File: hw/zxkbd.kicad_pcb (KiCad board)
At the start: 2 copper layers, 148 x 48 mm, 55 parts, among them J1 TAPE, J3 AY_IN, J4 SCART, J5 SERIAL, J6 ISP, Q1 BC846, SW1 RESET, SW2 MAGIC, SW3 AVR_RST, U1 74HC373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

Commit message: PCB first pass
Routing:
- net /D4: track 0.00 -> 183.7 mm, vias 0 -> 17
- net /KDA4: track 8.83 -> 128.7 mm, vias 0 -> 2
- net /KDB4: track 7.84 -> 112.5 mm, vias 0 -> 4
- net /KDB2: track 7.78 -> 103.0 mm, vias 0 -> 4
- net /KDA2: track 8.89 -> 100.4 mm, vias 0 -> 2
- net /KDD3: track 7.77 -> 99.1 mm, vias 0 -> 2
- net /KA0: track 3.39 -> 93.5 mm, vias 0 -> 2
- net /KA1: track 2.88 -> 89.2 mm, vias 0 -> 2
- net /KDA1: track 9.02 -> 92.0 mm, vias 0 -> 2
- net /PCLK: track 0.00 -> 75.1 mm, vias 0 -> 3
- net /KA3: track 3.38 -> 77.1 mm, vias 0 -> 2
- net /KDB1: track 7.90 -> 77.3 mm, vias 0 -> 2
- net /KDD2: track 7.64 -> 75.6 mm, vias 0 -> 4
- net /PDATA: track 0.00 -> 63.1 mm, vias 0 -> 1
- net /KDA0: track 8.98 -> 70.6 mm, vias 0 -> 2
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
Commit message: via stitching
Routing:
- net GND: track 3.99 -> 24.3 mm, vias 2 -> 65
- net /KDD3: track 99.1 -> 102.0 mm
- net /KA6: track 56.8 -> 59.4 mm
- net /D2: track 165.2 -> 167.1 mm
- net /KDE3: track 85.5 -> 87.4 mm
- net /KA2: track 49.5 -> 51.1 mm
- net /KDG3: track 51.4 -> 52.9 mm
- net /KDH3: track 41.4 -> 42.8 mm
- net /KDF3: track 74.0 -> 75.4 mm
- net /D1: track 172.3 -> 173.7 mm
- net /KDC0: track 45.0 -> 45.8 mm
- net /KA1: track 89.2 -> 90.1 mm
- net /KDB2: track 103.0 -> 103.8 mm
- net /KDH2: track 52.7 -> 53.5 mm
- net /KA3: track 77.1 -> 77.8 mm
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- added copper zone on B.Cu, net GND
- added copper zone on F.Cu, net GND

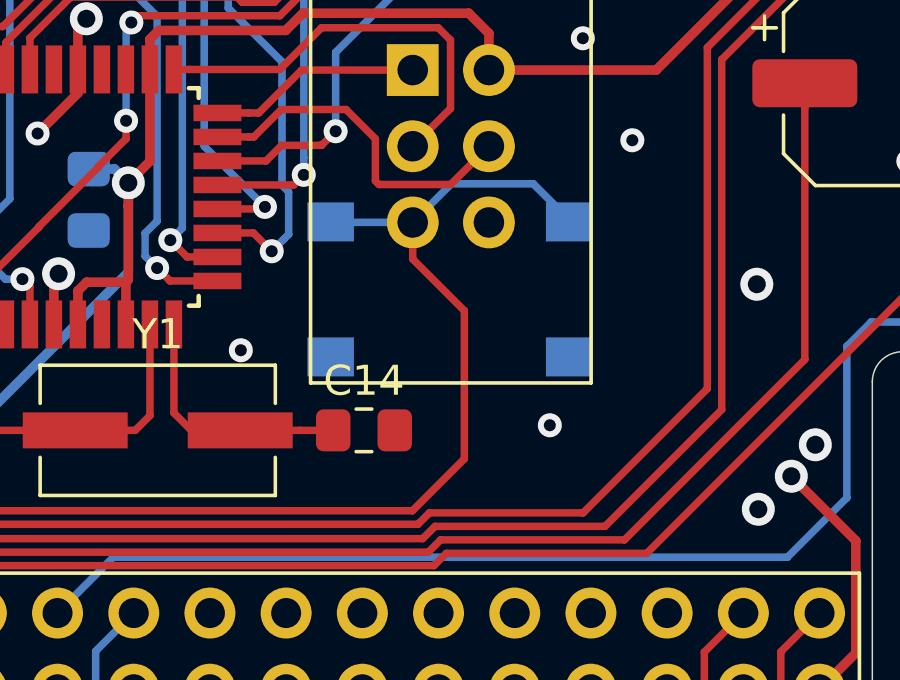
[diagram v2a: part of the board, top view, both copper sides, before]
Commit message: fixed PCB mistake, AVR reset switch overlapped with ISP header pins on the back side of the board.
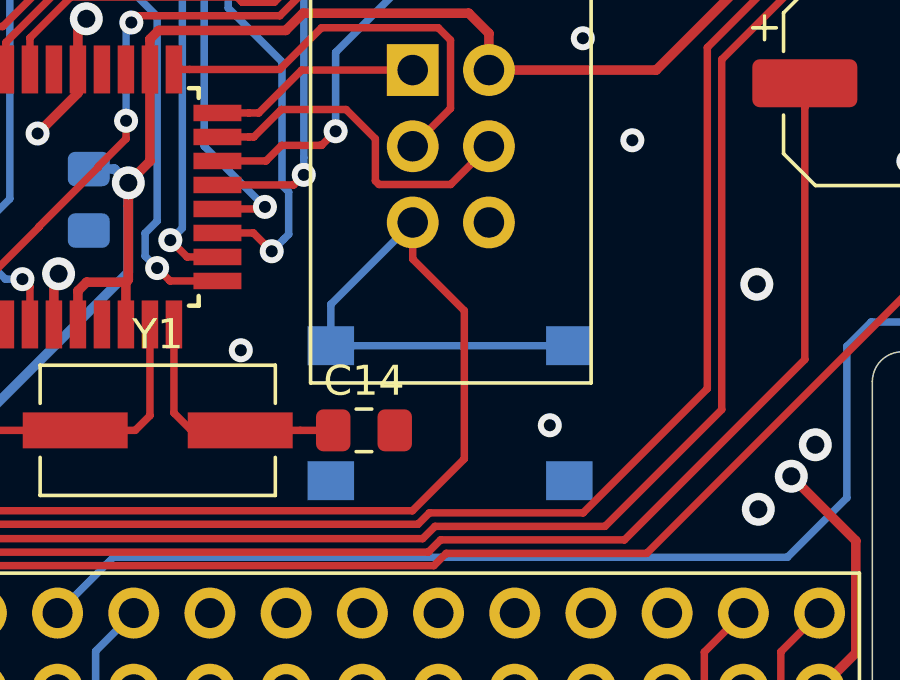
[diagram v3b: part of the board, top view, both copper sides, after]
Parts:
- moved SW3 4.13 mm to (174.4, 139.1)
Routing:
- net /~RESET: track 57.1 -> 61.3 mm
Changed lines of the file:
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@@
     (thickness 1.6)
     (drawings 13)
-    (tracks 2804)
+    (tracks 2801)
     (zones 0)
     (modules 55)
@@
   )
   (module Button_Switch_SMD:SW_Push_1P1T_NO_6x6mm_H9.5mm (layer B.Cu)
-    (at 174.42 134.92)
+    (at 174.425 139.05)
     (descr "tactile push button, 6x6mm e.g. PTS645xx series, height=9.5mm")
     (tags "tact sw push 6mm smd")
@@
   (segment (start 171.935002 131.305) (end 171.935002 129.901998) (width 0.25) (layer F.Cu) (net 23))
   (segment (start 174.445 131.425) (end 172.055002 131.425) (width 0.25) (layer F.Cu) (net 23))
-  (segment (start 170.465 132.69) (end 170.445 132.67) (width 0.25) (layer B.Cu) (net 24))
-  (segment (start 173.18 132.69) (end 170.465 132.69) (width 0.25) (layer B.Cu) (net 24))
   (segment (start 173.18 133.911314) (end 174.9 135.631314) (width 0.25) (layer F.Cu) (net 24))
   (segment (start 173.18 132.69) (end 173.18 133.911314) (width 0.25) (layer F.Cu) (net 24))
@@
   (segment (start 152.84 132.24) (end 158.17 132.24) (width 0.25) (layer F.Cu) (net 24))
   (segment (start 151.51 133.57) (end 152.84 132.24) (width 0.25) (layer F.Cu) (net 24))
-  (segment (start 178.41 132.61) (end 178.44 132.61) (width 0.25) (layer B.Cu) (net 24))
-  (segment (start 177.2 131.4) (end 178.41 132.61) (width 0.25) (layer B.Cu) (net 24))
-  (segment (start 173.18 132.69) (end 174.47 131.4) (width 0.25) (layer B.Cu) (net 24))
-  (segment (start 174.47 131.4) (end 177.2 131.4) (width 0.25) (layer B.Cu) (net 24))
+  (segment (start 170.45 135.42) (end 170.45 136.8) (width 0.25) (layer B.Cu) (net 24))
+  (segment (start 173.18 132.69) (end 170.45 135.42) (width 0.25) (layer B.Cu) (net 24))
+  (segment (start 170.45 136.8) (end 178.4 136.8) (width 0.25) (layer B.Cu) (net 24))
   (segment (start 202 117.4) (end 202 119.3) (width 0.25) (layer F.Cu) (net 25) (status 30))
   (segment (start 202 123.55) (end 202 121.2) (width 0.25) (layer F.Cu) (net 26) (status 30))

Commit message: finishing the pcb
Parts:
- added C15: 0.1uF, Capacitor_SMD:C_0805_2012Metric_Pad1.15x1.40mm_HandSolder, B.Cu at (86.6, 130.4)
- added C16: 0.1uF, Capacitor_SMD:C_0805_2012Metric_Pad1.15x1.40mm_HandSolder, B.Cu at (111.9, 132.6)
- added C17: 0.1uF, Capacitor_SMD:C_0805_2012Metric_Pad1.15x1.40mm_HandSolder, B.Cu at (133.6, 133.4)
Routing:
- net GND: track 24.3 -> 41.9 mm, vias 65 -> 73
- net VCC: track 505.1 -> 522.5 mm, vias 9 -> 12
- net /KDE0: track 38.3 -> 41.7 mm
- net /KDF0: track 29.7 -> 32.8 mm
- net /KDG0: track 68.6 -> 71.7 mm
- net /KDH0: track 80.9 -> 83.9 mm
- net /KDB4: track 112.5 -> 113.6 mm
- net /D0: track 183.8 -> 184.9 mm
- net /KA1: track 90.1 -> 89.0 mm
- net /SEL2: track 58.0 -> 58.7 mm
- net Net-(SW1-Pad2): track 140.2 -> 139.6 mm
- net /KDG3: track 52.9 -> 52.4 mm
- net /KDB3: track 111.7 -> 111.2 mm
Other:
- board text added: "AVR ISP"
- board text added: "GND"
- board text added: "RXD"
- board text added: "TXD"
- board text added: "VCC"
- board text added: "zxkbd rev 1"
- board text added: "zxkbd rev 1 Copyright © 2020 John Tsiombikas <nuclear@member.fsf.org> Creative Commons Attribution Share-Alike (CC BY-SA) https://github.com/jtsiomb/zxkbd"

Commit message: labels on the pcb
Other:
- board text added: "BLUE"
- board text added: "GREEN"
- board text added: "H+V SYNC"
- board text added: "KA3"
- board text added: "KA3-KA0"
- board text added: "KA4"
- board text added: "KA5"
- board text added: "KA6"
- board text added: "KA7"
- board text added: "KD0"
- board text added: "KD1"
- board text added: "KD2"
- board text added: "KD3"
- board text added: "KD4"
- board text added: "RED"
- board text added: "SOUND"
- board text added: "TAP IN"
- board text added: "TAP OUT"
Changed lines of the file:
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@@
   (general
     (thickness 1.6)
-    (drawings 20)
+    (drawings 43)
     (tracks 2889)
     (zones 0)
@@
     (tags "resistor array")
     (attr smd)
-    (fp_text reference RN6 (at 0 4.2 270) (layer B.SilkS)
+    (fp_text reference RN6 (at 0.8 -4.14 90) (layer B.SilkS)
       (effects (font (size 1 1) (thickness 0.15)) (justify mirror))
     )
-    (fp_text value 4k7 (at 0 -4.2 270) (layer B.Fab)
+    (fp_text value 4k7 (at 0 -0.04) (layer B.SilkS)
       (effects (font (size 1 1) (thickness 0.15)) (justify mirror))
     )
+    (fp_line (start 2.2 -3.45) (end -2.21 -3.45) (layer B.CrtYd) (width 0.05))
+    (fp_line (start 2.2 -3.45) (end 2.2 3.45) (layer B.CrtYd) (width 0.05))
+    (fp_line (start -2.21 3.45) (end -2.21 -3.45) (layer B.CrtYd) (width 0.05))
+    (fp_line (start -2.21 3.45) (end 2.2 3.45) (layer B.CrtYd) (width 0.05))
+    (fp_line (start 1.05 3.27) (end -1.05 3.27) (layer B.SilkS) (width 0.12))
+    (fp_line (start 1.05 -3.27) (end -1.05 -3.27) (layer B.SilkS) (width 0.12))
+    (fp_line (start -1.6 -3.2) (end -1.6 3.2) (layer B.Fab) (width 0.1))
+    (fp_line (start 1.6 -3.2) (end -1.6 -3.2) (layer B.Fab) (width 0.1))
+    (fp_line (start 1.6 3.2) (end 1.6 -3.2) (layer B.Fab) (width 0.1))
+    (fp_line (start -1.6 3.2) (end 1.6 3.2) (layer B.Fab) (width 0.1))
     (fp_text user %R (at 0 0) (layer B.Fab)
       (effects (font (size 1 1) (thickness 0.15)) (justify mirror))
     )
-    (fp_line (start -1.6 3.2) (end 1.6 3.2) (layer B.Fab) (width 0.1))
-    (fp_line (start 1.6 3.2) (end 1.6 -3.2) (layer B.Fab) (width 0.1))
-    (fp_line (start 1.6 -3.2) (end -1.6 -3.2) (layer B.Fab) (width 0.1))
-    (fp_line (start -1.6 -3.2) (end -1.6 3.2) (layer B.Fab) (width 0.1))
-    (fp_line (start 1.05 -3.27) (end -1.05 -3.27) (layer B.SilkS) (width 0.12))
-    (fp_line (start 1.05 3.27) (end -1.05 3.27) (layer B.SilkS) (width 0.12))
-    (fp_line (start -2.21 3.45) (end 2.2 3.45) (layer B.CrtYd) (width 0.05))
-    (fp_line (start -2.21 3.45) (end -2.21 -3.45) (layer B.CrtYd) (width 0.05))
-    (fp_line (start 2.2 -3.45) (end 2.2 3.45) (layer B.CrtYd) (width 0.05))
-    (fp_line (start 2.2 -3.45) (end -2.21 -3.45) (layer B.CrtYd) (width 0.05))
-    (pad 1 smd rect (at -1.5 2.6 90) (size 0.9 0.9) (layers B.Cu B.Paste B.Mask)
-      (net 69 /KA0))
-    (pad 5 smd rect (at -1.5 -2.6 90) (size 0.9 0.9) (layers B.Cu B.Paste B.Mask)
-      (net 2 VCC))
-    (pad 2 smd rect (at -1.5 1.28 90) (size 0.9 0.9) (layers B.Cu B.Paste B.Mask)
-      (net 70 /KA1))
-    (pad 4 smd rect (at -1.5 -1.28 90) (size 0.9 0.9) (layers B.Cu B.Paste B.Mask)
-      (net 71 /KA3))
-    (pad 3 smd rect (at -1.5 0 90) (size 0.9 0.9) (layers B.Cu B.Paste B.Mask)
-      (net 72 /KA2))
-    (pad 7 smd rect (at 1.5 -1.28 90) (size 0.9 0.9) (layers B.Cu B.Paste B.Mask)
-      (net 73 /KA5))
-    (pad 10 smd rect (at 1.5 2.6 90) (size 0.9 0.9) (layers B.Cu B.Paste B.Mask))
-    (pad 6 smd rect (at 1.5 -2.6 90) (size 0.9 0.9) (layers B.Cu B.Paste B.Mask)
-      (net 74 /KA4))
-    (pad 9 smd rect (at 1.5 1.28 90) (size 0.9 0.9) (layers B.Cu B.Paste B.Mask)
-      (net 75 /KA7))
     (pad 8 smd rect (at 1.5 0 90) (size 0.9 0.9) (layers B.Cu B.Paste B.Mask)
       (net 76 /KA6))
+    (pad 9 smd rect (at 1.5 1.28 90) (size 0.9 0.9) (layers B.Cu B.Paste B.Mask)
+      (net 75 /KA7))
+    (pad 6 smd rect (at 1.5 -2.6 90) (size 0.9 0.9) (layers B.Cu B.Paste B.Mask)
+      (net 74 /KA4))
+    (pad 10 smd rect (at 1.5 2.6 90) (size 0.9 0.9) (layers B.Cu B.Paste B.Mask))
+    (pad 7 smd rect (at 1.5 -1.28 90) (size 0.9 0.9) (layers B.Cu B.Paste B.Mask)
+      (net 73 /KA5))
+    (pad 3 smd rect (at -1.5 0 90) (size 0.9 0.9) (layers B.Cu B.Paste B.Mask)
+      (net 72 /KA2))
+    (pad 4 smd rect (at -1.5 -1.28 90) (size 0.9 0.9) (layers B.Cu B.Paste B.Mask)
+      (net 71 /KA3))
+    (pad 2 smd rect (at -1.5 1.28 90) (size 0.9 0.9) (layers B.Cu B.Paste B.Mask)
+      (net 70 /KA1))
+    (pad 5 smd rect (at -1.5 -2.6 90) (size 0.9 0.9) (layers B.Cu B.Paste B.Mask)
+      (net 2 VCC))
+    (pad 1 smd rect (at -1.5 2.6 90) (size 0.9 0.9) (layers B.Cu B.Paste B.Mask)
+      (net 69 /KA0))
     (model ${KISYS3DMOD}/Resistor_SMD.3dshapes/R_Array_Convex_5x1206.wrl
       (at (xyz 0 0 0))
@@
     )
   )
+  (gr_text "TAP OUT" (at 187.3 141.2 270) (layer B.SilkS)
+    (effects (font (size 1 1) (thickness 0.15)) (justify mirror))
+  )
+  (gr_text "TAP IN" (at 183.5 141.9 270) (layer B.SilkS)
+    (effects (font (size 1 1) (thickness 0.15)) (justify mirror))
+  )
+  (gr_text SOUND (at 161.3 141.8 270) (layer B.SilkS)
+    (effects (font (size 1 1) (thickness 0.15)) (justify mirror))
+  )
+  (gr_text GREEN (at 153.7 142 270) (layer B.SilkS)
+    (effects (font (size 1 1) (thickness 0.15)) (justify mirror))
+  )
+  (gr_text BLUE (at 151.1 142.6 270) (layer B.SilkS)
+    (effects (font (size 1 1) (thickness 0.15)) (justify mirror))
+  )
+  (gr_text RED (at 148.6 143 270) (layer B.SilkS)
+    (effects (font (size 1 1) (thickness 0.15)) (justify mirror))
+  )
+  (gr_text "H+V SYNC" (at 146.1 140.6 270) (layer B.SilkS)
+    (effects (font (size 1 1) (thickness 0.15)) (justify mirror))
+  )
+  (gr_text KD0 (at 138.5 143 270) (layer B.SilkS)
+    (effects (font (size 1 1) (thickness 0.15)) (justify mirror))
+  )
+  (gr_text KD1 (at 135.9 143 270) (layer B.SilkS)
+    (effects (font (size 1 1) (thickness 0.15)) (justify mirror))
+  )
+  (gr_text KD2 (at 133.3 143 270) (layer B.SilkS)
+    (effects (font (size 1 1) (thickness 0.15)) (justify mirror))
+  )
+  (gr_text KD4 (at 130.9 143 270) (layer B.SilkS)
+    (effects (font (size 1 1) (thickness 0.15)) (justify mirror))
+  )
+  (gr_text KD3 (at 128.3 143 270) (layer B.SilkS)
+    (effects (font (size 1 1) (thickness 0.15)) (justify mirror))
+  )
+  (gr_text KA7 (at 125.8 143.1 270) (layer B.SilkS)
+    (effects (font (size 1 1) (thickness 0.15)) (justify mirror))
+  )
+  (gr_text KA3 (at 105.8 145.6 270) (layer B.SilkS)
+    (effects (font (size 1 1) (thickness 0.15)) (justify mirror))
+  )
+  (gr_text KA6 (at 123.3 143.1 270) (layer B.SilkS)
+    (effects (font (size 1 1) (thickness 0.15)) (justify mirror))
+  )
+  (gr_text KA5 (at 120.7 143.1 270) (layer B.SilkS)
+    (effects (font (size 1 1) (thickness 0.15)) (justify mirror))
+  )
+  (gr_text KA4 (at 118.2 143.1 270) (layer B.SilkS)
+    (effects (font (size 1 1) (thickness 0.15)) (justify mirror))
+  )
+  (gr_line (start 107.3 144.4) (end 107 144.7) (layer B.SilkS) (width 0.12))
+  (gr_line (start 116.3 144.4) (end 116.6 144.8) (layer B.SilkS) (width 0.12))
+  (gr_line (start 107.3 144.3) (end 116.3 144.4) (layer B.SilkS) (width 0.12))
+  (gr_line (start 107 143.8) (end 107.3 144.3) (layer B.SilkS) (width 0.12))
+  (gr_line (start 100.4 143.8) (end 107 143.8) (layer B.SilkS) (width 0.12))
+  (gr_text KA3-KA0 (at 103.6 143.1) (layer B.SilkS)
+    (effects (font (size 1 1) (thickness 0.15)) (justify mirror))
+  )
   (gr_text GND (at 150.9 138.6) (layer F.SilkS)

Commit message: PCB completed
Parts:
- added J2: LINEOUT, zxkbd:cui_sj1-3525ng, F.Cu at (222.3, 129.6)
- added REF**: OSHW-Logo2_9.8x8mm_SilkScreen, Symbol:OSHW-Logo2_9.8x8mm_SilkScreen, B.Cu at (166.1, 120.5)
- added REF**: OSHW-Logo2_9.8x8mm_SilkScreen, Symbol:OSHW-Logo2_9.8x8mm_SilkScreen, F.Cu at (143.8, 130.5)
- moved J3 39.7 mm to (183.5, 132.4), turned to 0 degrees
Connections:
- U8 pad A2: (no net) -> VCC
- U8 pad A27: (no net) -> GND
- U8 pad A28: (no net) -> GND
- U8 pad A29: (no net) -> GND
- U8 pad A30: (no net) -> GND
- U8 pad A31: (no net) -> GND
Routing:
- net /A_R: track 9.69 -> 22.9 mm
- net /GREEN: track 45.1 -> 53.3 mm
- net /A_L: track 9.84 -> 16.5 mm
- net Net-(J3-Pad1): track 28.2 -> 22.8 mm
- net Net-(J3-Pad3): track 18.9 -> 22.9 mm
- net VCC: track 522.5 -> 525.1 mm
- net /RED: track 61.0 -> 59.5 mm
- net /HVSYNC: track 72.6 -> 71.4 mm
- net /SOUND: track 56.4 -> 57.3 mm
- net GND: vias 73 -> 75
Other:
- board size 148 x 48 mm -> 148.3 x 48 mm
- board text added: "AU_IN"
- board text added: "AU_L"
- board text added: "AU_R"
- board text added: "AVR RESET"
- board text added: "CLK"
- board text added: "DATA"
- board text added: "L"
- board text added: "MAGIC"
- board text added: "PS/2 keyb"
- board text added: "Pentagon128k connector"
- board text added: "R"
- board text added: "RESET"
- board text added: "SCART"
- board text added: "SERIAL"
- board text added: "SYNC"
- board text added: "VCC AU_L AU_R GND GND"
- board text added: "VCC SYNC RED BLU GRN"
- board text added: "zxkbd rev 1 Copyright © 2020 John Tsiombikas <nuclear@member.fsf.org> Creative Commons Attribution Share-Alike"
- board text removed: "zxkbd rev 1"
